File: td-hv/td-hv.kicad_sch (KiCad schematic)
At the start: 57 parts, among them J1 Conn_01x07_Male, Q1 IMBF170R450M1XTMA1, U2 TLC272, U3 LM2903

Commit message: td-hv improvements
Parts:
- removed Q1: IMBF170R450M1XTMA1, Package_TO_SOT_SMD:TO-263-7_TabPin8, symbol Transistor_FET:C2M1000170J
- removed Q?: BC847, Package_TO_SOT_SMD:SOT-23, symbol Transistor_BJT:BC847
- removed R? (x6): 10k, symbol Device:R
- removed U?: TLC272, Package_SO:SOIC-8_3.9x4.9mm_P1.27mm, symbol Amplifier_Operational:TLC272
- added C?: 0.01uF, Capacitor_SMD:C_0805_2012Metric, symbol Device:C
- added C?: 0.1uF, Capacitor_SMD:C_0805_2012Metric, symbol Device:C
- added L?: 50uH, symbol Device:L
- added Q?: MSC750SMA170S, Package_TO_SOT_SMD:TO-268-2, symbol Transistor_FET:STD7NK40Z
- added Q?: BC857, Package_TO_SOT_SMD:SOT-23, symbol Transistor_BJT:BC857
- added R?: 10 10W, symbol Device:R
- added R?: 10k, Resistor_SMD:R_0805_2012Metric, symbol Device:R
- added R?: 24, symbol Device:R
- added R?: 470, Resistor_SMD:R_0805_2012Metric, symbol Device:R
- added R?: 47 10W, symbol Device:R
- added unit 3 of U2
- added unit 2 of U2
- C11: value 0.1uF -> 0.01uF; Digikey 478-10836-1-ND -> (none)
- C14: value 0.1uF -> DNP
- R19: value 100k -> DNP
- R5: value 100k -> 47k; Digikey YAG3688CT-ND -> (none)
- R?: value 10k -> 20k
- RV2: value 1k -> 47k
- U2: footprint Package_SO:SOIC-8_3.9x4.9mm_P1.27mm -> (none); symbol Amplifier_Operational:TLC272 -> Amplifier_Operational:TLC274
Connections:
- net ss is gone; now on net comp: U3.1
- net +5V: now also U2.4 (V+), R?.2; no longer RV2.3, U2.8 (V+)
- net GND: now also R5.2, U2.11 (V-), C?.2, C?.2, Q?.2 (E), R?.2, R?.2; no longer C?.2, R20.2, RV1.3, RV2.1, U2.4 (V-)
- net VBUS: now also R?.1; no longer C4.1, C5.1, L1.2, R10.1, R9.1
- net fb: now also C14.2, R20.2, U?.2 (FB); no longer J1.6 (Pin_6), U2.1
- net sw: now also Q?.2 (D)
- net at R18.2: now also Q?.1 (G)
- net at R17.1, R4.1: now also Q?.3 (S)
- net at RV2.2, U2.3 (+): now also R5.1, RV2.1, C?.1
- net comp: now reaches U?.1 (COMP)
- net comp: now also C12.2, R14.2, Q?.3 (C)
- net at C?.1, R?.1, U?.4 (RC): now also U2.10 (+)
- net at R?.2: now also U2.8, U2.9 (-)
- new net: L1.2, L?.2, R10.1, R?.2
- new net: L1.7, RV2.3
- new net: C4.1, C5.1, L?.1, R9.1, R?.1, R?.2
- new net: R?.1, RV1.3
- new net: R19.1, R20.1, U2.1, U2.2 (-), U2.5 (+)
- new net: C?.1, Q?.1 (B), R?.1
- new net: C?.2, R?.1
- new net eht_voltage: J1.6 (Pin_6), U2.6 (-), U2.7
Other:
- note added: "maximum setting for protection is ~38kV"
- note added: "todo: add pin 10 to sheet symbol of flyback remove voltage offset from rc->cs which limits min duty cycle fix labels on deflection board connector tune compensation determine if type III compensation is needed investigate damping options"
- note removed: "todo: make x-ray protect actually shut down add pin 10 to sheet symbol of flyback remove voltage offset from rc->cs which limits min duty cycle don't needlessly use multiple op amps in series fix voltage output pin fix labels on deflection board connector tune compensation determine if type III compensation is needed check cs amplitude investigate damping options"
- moved on the sheet: C11, C12, C14, C4, C5, R14, R19, R9, R?, RV2, U2A

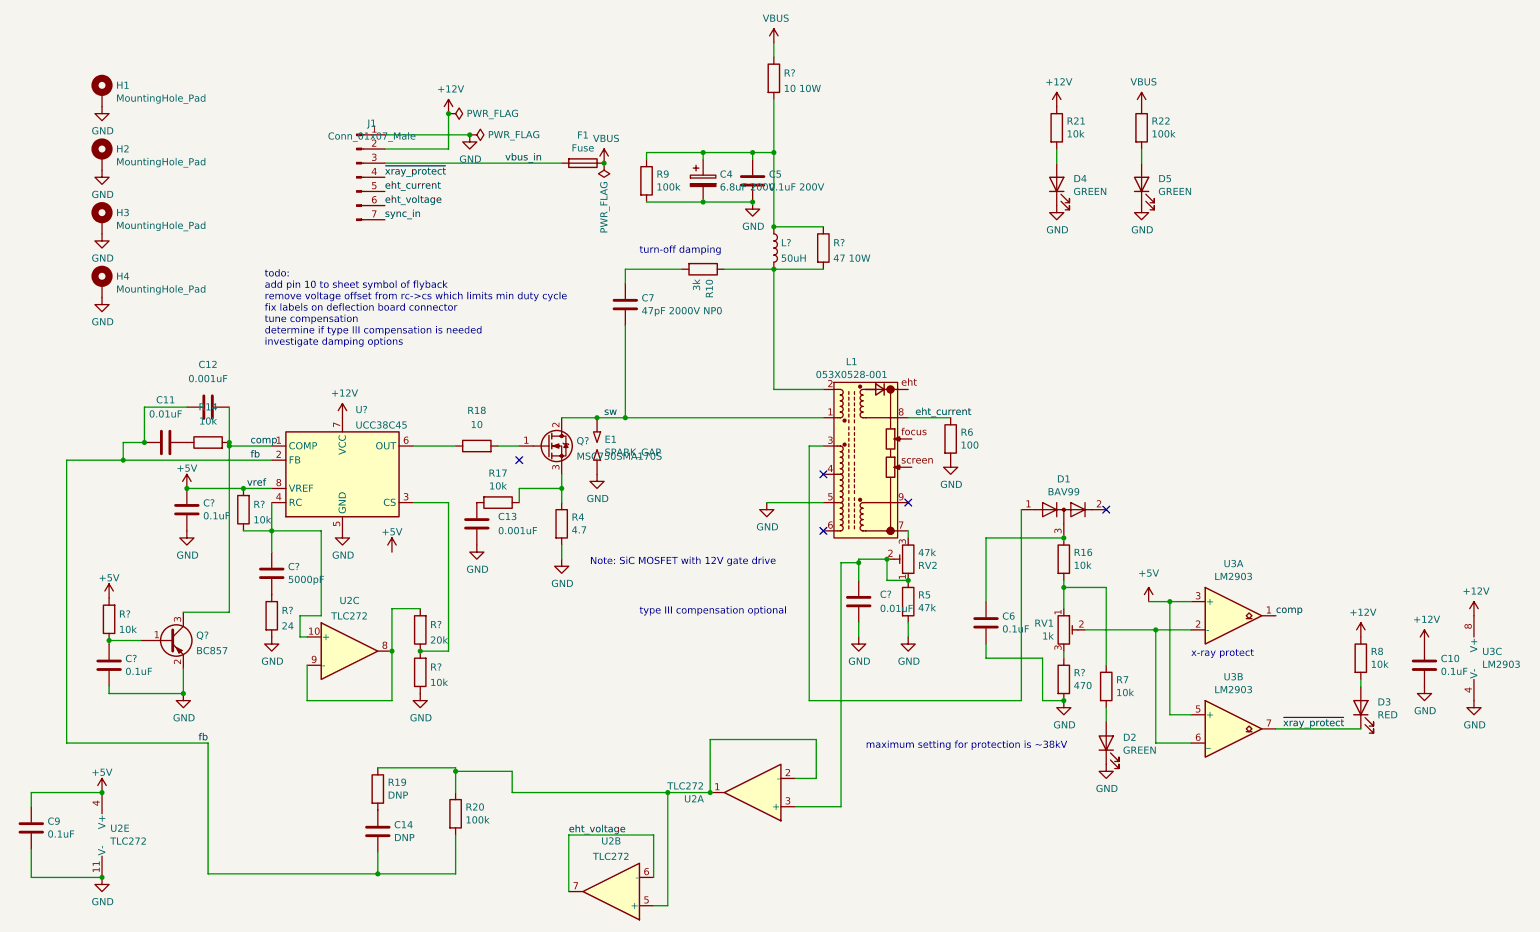
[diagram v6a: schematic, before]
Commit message: new version of td-hv, microcontroller control only
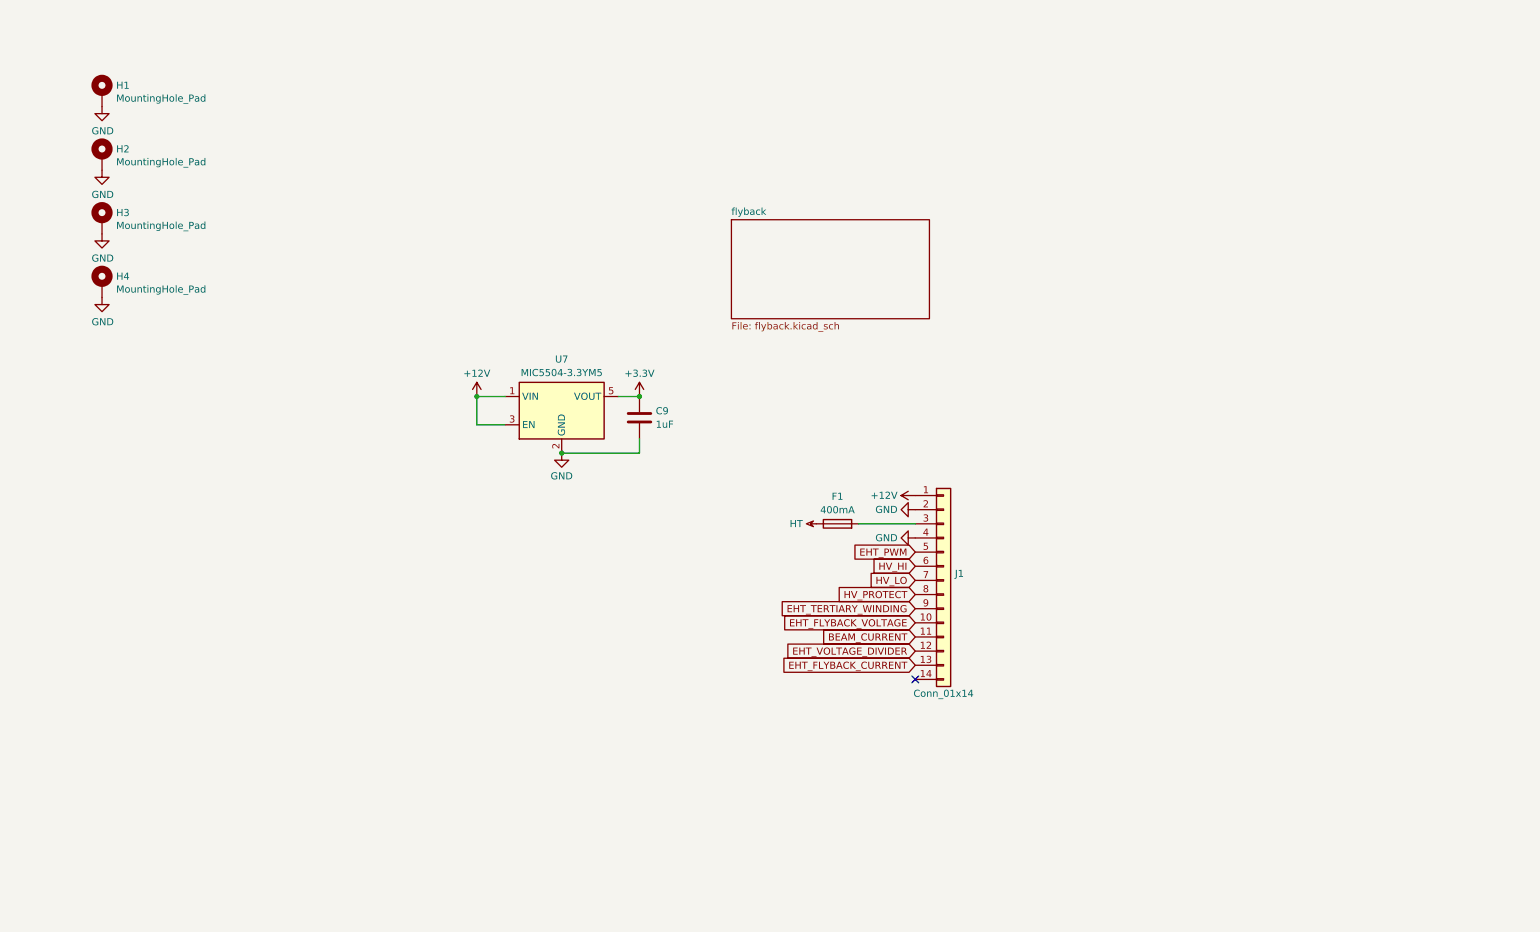
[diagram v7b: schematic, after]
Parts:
- removed C10, C6, C? (x2): 0.1uF, Capacitor_SMD:C_0805_2012Metric, symbol Device:C
- removed C11, C?: 0.01uF, Capacitor_SMD:C_0805_2012Metric, symbol Device:C
- removed C12, C13: 0.001uF, Capacitor_SMD:C_0805_2012Metric, symbol Device:C
- removed C14: DNP, Capacitor_SMD:C_0805_2012Metric, symbol Device:C
- removed C4: 6.8uF 200V, Capacitor_SMD:C_Elec_8x10.2, symbol Device:C_Polarized
- removed C5: 0.1uF 200V, Capacitor_SMD:C_1206_3216Metric, symbol Device:C
- removed C7: 47pF 2000V NP0, Capacitor_SMD:C_1206_3216Metric, symbol Device:C
- removed C?: 5000pF, Capacitor_SMD:C_0805_2012Metric, symbol Device:C
- removed D1: BAV99, Package_TO_SOT_SMD:SOT-23, symbol Diode:BAV99
- removed D2: GREEN, LED_SMD:LED_0805_2012Metric_Castellated, symbol Device:LED
- removed D3: RED, LED_SMD:LED_0805_2012Metric_Castellated, symbol Device:LED
- removed D4, D5: GREEN, LED_SMD:LED_0805_2012Metric, symbol Device:LED
- removed E1: SPARK_GAP, Resistor_SMD:R_1218_3246Metric_Pad1.22x4.75mm_HandSolder, symbol Device:SparkGap
- removed J1: Conn_01x07_Male, Connector_JST:JST_XH_B7B-XH-AM_1x07_P2.50mm_Vertical, symbol Connector:Conn_01x07_Male
- removed L1: 053X0528-001, td-hv:053X0528-001, symbol td-hv:053X0528-001
- removed L?: 50uH, symbol Device:L
- removed Q?: MSC750SMA170S, Package_TO_SOT_SMD:TO-268-2, symbol Transistor_FET:STD7NK40Z
- removed Q?: BC857, Package_TO_SOT_SMD:SOT-23, symbol Transistor_BJT:BC857
- removed R10: 3k, Resistor_SMD:R_2512_6332Metric, symbol Device:R
- removed R14, R16, R17, R21, R7, R8, R?: 10k, Resistor_SMD:R_0805_2012Metric, symbol Device:R
- removed R18: 10, Resistor_SMD:R_0805_2012Metric, symbol Device:R
- removed R19: DNP, Resistor_SMD:R_0805_2012Metric, symbol Device:R
- removed R20, R22: 100k, Resistor_SMD:R_0805_2012Metric, symbol Device:R
- removed R4: 4.7, Resistor_SMD:R_1206_3216Metric, symbol Device:R
- removed R5: 47k, Resistor_SMD:R_0805_2012Metric, symbol Device:R
- removed R6: 100, Resistor_SMD:R_0805_2012Metric, symbol Device:R
- removed R9: 100k, Resistor_SMD:R_1210_3225Metric, symbol Device:R
- removed R?: 10 10W, symbol Device:R
- removed R? (x2): 10k, symbol Device:R
- removed R?: 24, symbol Device:R
- removed R?: 470, Resistor_SMD:R_0805_2012Metric, symbol Device:R
- removed R?: 47 10W, symbol Device:R
- removed R?: 20k, symbol Device:R
- removed RV1: 1k, Potentiometer_SMD:Potentiometer_Bourns_3314G_Vertical, symbol Device:R_Potentiometer_Trim
- removed RV2: 47k, Potentiometer_SMD:Potentiometer_Bourns_3314G_Vertical, symbol Device:R_Potentiometer_Trim
- removed U2: TLC272, symbol Amplifier_Operational:TLC274
- removed U3: LM2903, Package_SO:SOIC-8_3.9x4.9mm_P1.27mm, symbol Comparator:LM2903
- removed U?: UCC38C45, Package_SO:SOIC-8_3.9x4.9mm_P1.27mm, symbol Regulator_Controller:UC3845_SOIC8
- added J1: Conn_01x14, Connector_JST:JST_XH_B14B-XH-A_1x14_P2.50mm_Vertical, symbol Connector_Generic:Conn_01x14
- added U7: MIC5504-3.3YM5, Package_TO_SOT_SMD:SOT-23-5, symbol Regulator_Linear:MIC5504-3.3YM5
- C9: value 0.1uF -> 1uF; Digikey 478-10836-1-ND -> 311-1365-1-ND
- F1: value Fuse -> 400mA; footprint Fuse:Fuse_Schurter_UMT250 -> Fuse:Fuse_Schurter_UMZ250; Digikey F1889-ND -> 486-4326-ND
- H1, H2, H3, H4: Digikey (none) -> DNP
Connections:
- net +12V: now also J1.1 (Pin_1), U7.1 (VIN), U7.3 (EN)
- net GND: now also J1.2 (Pin_2), J1.4 (Pin_4), U7.2 (GND)
- net +5V renamed +3.3V
- net +3.3V: now also U7.5 (VOUT)
- net VBUS renamed HT
- net vbus_in: no longer names the net of F1.2
- net vbus_in: now also J1.3 (Pin_3)
- new net BEAM_CURRENT: J1.11 (Pin_11)
- new net EHT_FLYBACK_CURRENT: J1.13 (Pin_13)
- new net EHT_FLYBACK_VOLTAGE: J1.10 (Pin_10)
- new net EHT_PWM: J1.5 (Pin_5)
- new net EHT_TERTIARY_WINDING: J1.9 (Pin_9)
- new net EHT_VOLTAGE_DIVIDER: J1.12 (Pin_12)
- new net HV_HI: J1.6 (Pin_6)
- new net HV_LO: J1.7 (Pin_7)
- new net HV_PROTECT: J1.8 (Pin_8)
- no-connect marks 5 -> 1
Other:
- added sheet flyback (flyback.kicad_sch)
- note removed: "Note: SiC MOSFET with 12V gate drive"
- note removed: "maximum setting for protection is ~38kV"
- note removed: "todo: add pin 10 to sheet symbol of flyback remove voltage offset from rc->cs which limits min duty cycle fix labels on deflection board connector tune compensation determine if type III compensation is needed investigate damping options"
- note removed: "turn-off damping"
- note removed: "type III compensation optional"
- note removed: "x-ray protect"

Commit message: td-hv 2.0 changes
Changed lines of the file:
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@@
   (junction (at 114.3 91.44) (diameter 0) (color 0 0 0 0)
   )
+  (junction (at 154.94 104.14) (diameter 0) (color 0 0 0 0)
+  )
   (junction (at 128.27 81.28) (diameter 0) (color 0 0 0 0)
   )
+  (junction (at 99.06 86.36) (diameter 0) (color 0 0 0 0)
+  )
   (junction (at 99.06 81.28) (diameter 0) (color 0 0 0 0)
+  )
+  (junction (at 128.27 91.44) (diameter 0) (color 0 0 0 0)
   )
   (no_connect (at 177.8 132.08))
@@
     (stroke (width 0) (type default))
   )
+  (wire (pts (xy 151.13 104.14) (xy 154.94 104.14))
+    (stroke (width 0) (type default))
+  )
   (wire (pts (xy 114.3 91.44) (xy 128.27 91.44))
     (stroke (width 0) (type default))
@@
     (stroke (width 0) (type default))
   )
+  (wire (pts (xy 154.94 104.14) (xy 160.02 104.14))
+    (stroke (width 0) (type default))
+  )
   (wire (pts (xy 128.27 91.44) (xy 128.27 88.9))
     (stroke (width 0) (type default))
@@
     )
   )
-  (symbol (lib_name "GND_1") (lib_id "power:GND") (at 177.8 101.6 270) (unit 1)
+  (symbol (lib_id "power:GND") (at 177.8 101.6 270) (unit 1)
     (in_bom yes) (on_board yes) (dnp no) (fields_autoplaced)
     (property "Reference" "#PWR029" (at 171.45 101.6 0)
@@
         (path "/df1899ac-6757-4b81-9bb4-d715572ccf8c"
           (reference "F1") (unit 1)
+        )
+      )
+    )
+  )
+  (symbol (lib_id "power:PWR_FLAG") (at 128.27 91.44 270) (unit 1)
+    (in_bom yes) (on_board yes) (dnp no) (fields_autoplaced)
+    (property "Reference" "#FLG01" (at 130.175 91.44 0)
+      (effects (font (size 1.27 1.27)) hide)
+    )
+    (property "Value" "PWR_FLAG" (at 131.445 91.44 90)
+      (effects (font (size 1.27 1.27)) (justify left))
+    )
+    (property "Footprint" "" (at 128.27 91.44 0)
+      (effects (font (size 1.27 1.27)) hide)
+    )
+    (property "Datasheet" "~" (at 128.27 91.44 0)
+      (effects (font (size 1.27 1.27)) hide)
+    )
+    (pin "1")
+    (instances
+      (project "td-hv"
+        (path "/df1899ac-6757-4b81-9bb4-d715572ccf8c"
+          (reference "#FLG01") (unit 1)
         )
       )
@@
     )
   )
+  (symbol (lib_id "power:PWR_FLAG") (at 99.06 86.36 90) (unit 1)
+    (in_bom yes) (on_board yes) (dnp no) (fields_autoplaced)
+    (property "Reference" "#FLG02" (at 97.155 86.36 0)
+      (effects (font (size 1.27 1.27)) hide)
+    )
+    (property "Value" "PWR_FLAG" (at 95.8851 86.36 90)
+      (effects (font (size 1.27 1.27)) (justify left))
+    )
+    (property "Footprint" "" (at 99.06 86.36 0)
+      (effects (font (size 1.27 1.27)) hide)
+    )
+    (property "Datasheet" "~" (at 99.06 86.36 0)
+      (effects (font (size 1.27 1.27)) hide)
+    )
+    (pin "1")
+    (instances
+      (project "td-hv"
+        (path "/df1899ac-6757-4b81-9bb4-d715572ccf8c"
+          (reference "#FLG02") (unit 1)
+        )
+      )
+    )
+  )
   (symbol (lib_id "Device:C") (at 128.27 85.09 0) (unit 1)
     (in_bom yes) (on_board yes) (dnp no) (fields_autoplaced)
@@
     )
   )
-  (symbol (lib_id "power:HT") (at 160.02 104.14 90) (unit 1)
-    (in_bom yes) (on_board yes) (dnp no) (fields_autoplaced)
-    (property "Reference" "#PWR030" (at 156.972 104.14 0)
-      (effects (font (size 1.27 1.27)) hide)
-    )
-    (property "Value" "HT" (at 157.6071 104.14 90)
-      (effects (font (size 1.27 1.27)) (justify left))
-    )
-    (property "Footprint" "" (at 160.02 104.14 0)
-      (effects (font (size 1.27 1.27)) hide)
-    )
-    (property "Datasheet" "" (at 160.02 104.14 0)
+  (symbol (lib_id "power:PWR_FLAG") (at 154.94 104.14 0) (unit 1)
+    (in_bom yes) (on_board yes) (dnp no) (fields_autoplaced)
+    (property "Reference" "#FLG03" (at 154.94 102.235 0)
+      (effects (font (size 1.27 1.27)) hide)
+    )
+    (property "Value" "PWR_FLAG" (at 154.94 100.0069 0)
+      (effects (font (size 1.27 1.27)))
+    )
+    (property "Footprint" "" (at 154.94 104.14 0)
+      (effects (font (size 1.27 1.27)) hide)
+    )
+    (property "Datasheet" "~" (at 154.94 104.14 0)
+      (effects (font (size 1.27 1.27)) hide)
+    )
+    (pin "1")
+    (instances
+      (project "td-hv"
+        (path "/df1899ac-6757-4b81-9bb4-d715572ccf8c"
+          (reference "#FLG03") (unit 1)
+        )
+      )
+    )
+  )
+  (symbol (lib_id "power:HT") (at 151.13 104.14 90) (unit 1)
+    (in_bom yes) (on_board yes) (dnp no) (fields_autoplaced)
+    (property "Reference" "#PWR030" (at 148.082 104.14 0)
+      (effects (font (size 1.27 1.27)) hide)
+    )
+    (property "Value" "HT" (at 148.7171 104.14 90)
+      (effects (font (size 1.27 1.27)) (justify left))
+    )
+    (property "Footprint" "" (at 151.13 104.14 0)
+      (effects (font (size 1.27 1.27)) hide)
+    )
+    (property "Datasheet" "" (at 151.13 104.14 0)
       (effects (font (size 1.27 1.27)) hide)
     )
@@
     )
   )
-  (symbol (lib_name "GND_2") (lib_id "power:GND") (at 177.8 106.68 270) (unit 1)
+  (symbol (lib_id "power:GND") (at 177.8 106.68 270) (unit 1)
     (in_bom yes) (on_board yes) (dnp no) (fields_autoplaced)
     (property "Reference" "#PWR031" (at 171.45 106.68 0)
@@
     )
   )
-  (symbol (lib_name "GND_3") (lib_id "power:GND") (at 114.3 91.44 0) (unit 1)
+  (symbol (lib_id "power:GND") (at 114.3 91.44 0) (unit 1)
     (in_bom yes) (on_board yes) (dnp no) (fields_autoplaced)
     (property "Reference" "#PWR032" (at 114.3 97.79 0)
